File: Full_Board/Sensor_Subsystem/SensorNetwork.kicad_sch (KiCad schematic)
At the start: 32 parts, among them IC5 CD74HC4051PWT, IC6 CD74HC4051PWT, J10 OQ0432500000G, J11 OQ0432500000G, J12 OQ0432500000G, J13 OQ0432500000G, J14 OQ0432500000G, J15 OQ0432500000G, J16 OQ0432500000G, J17 OQ0432500000G, U10 UCLAMP3301H.TCT, U11 UCLAMP3301H.TCT

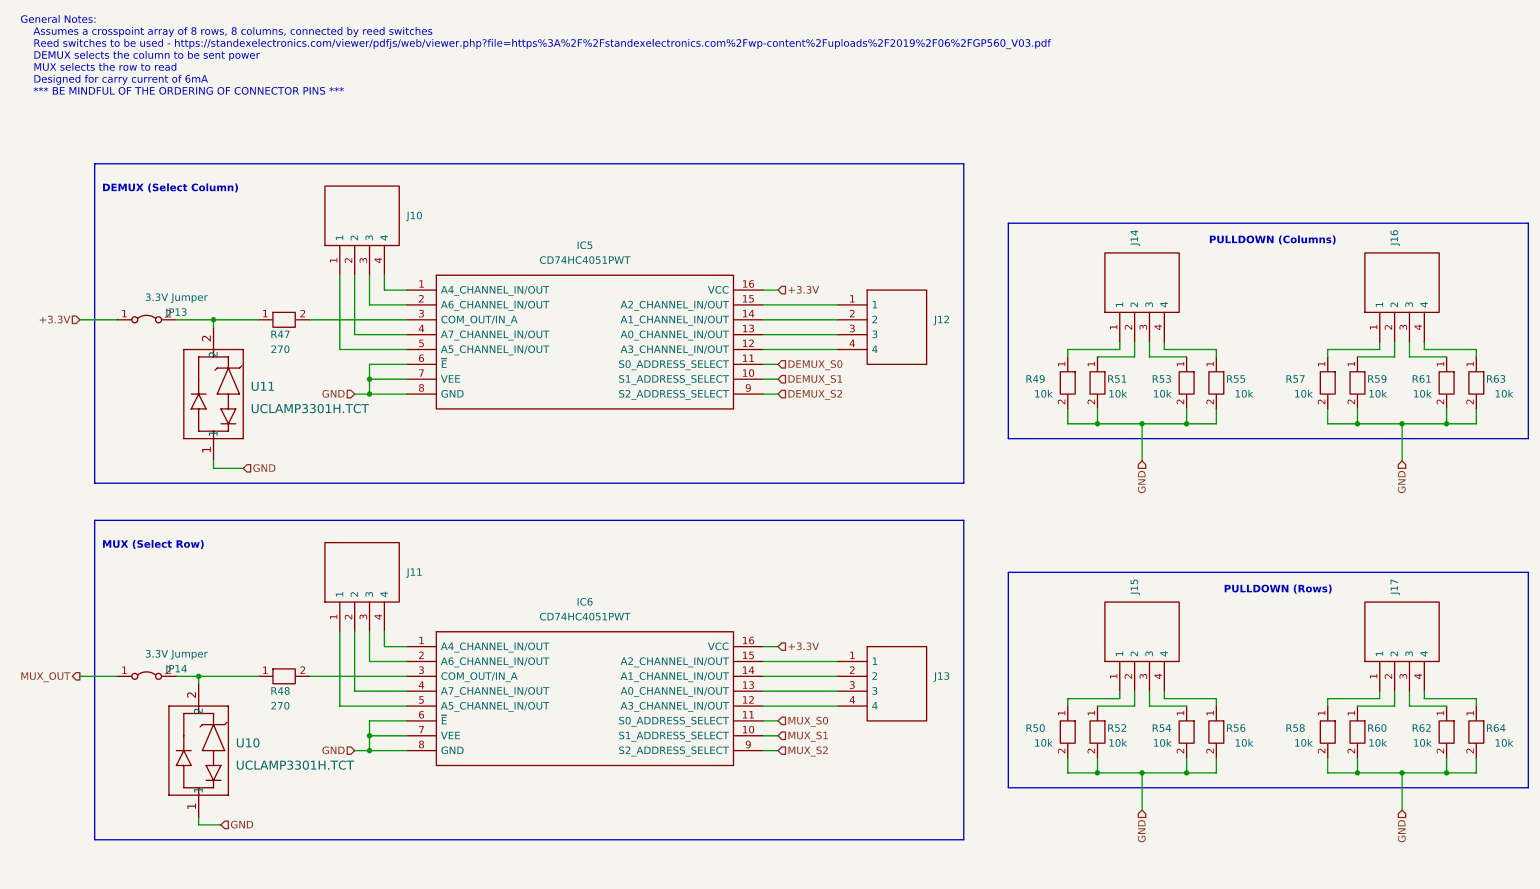
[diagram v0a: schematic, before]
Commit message: Redo pinout, finish pcb layout (no traces)
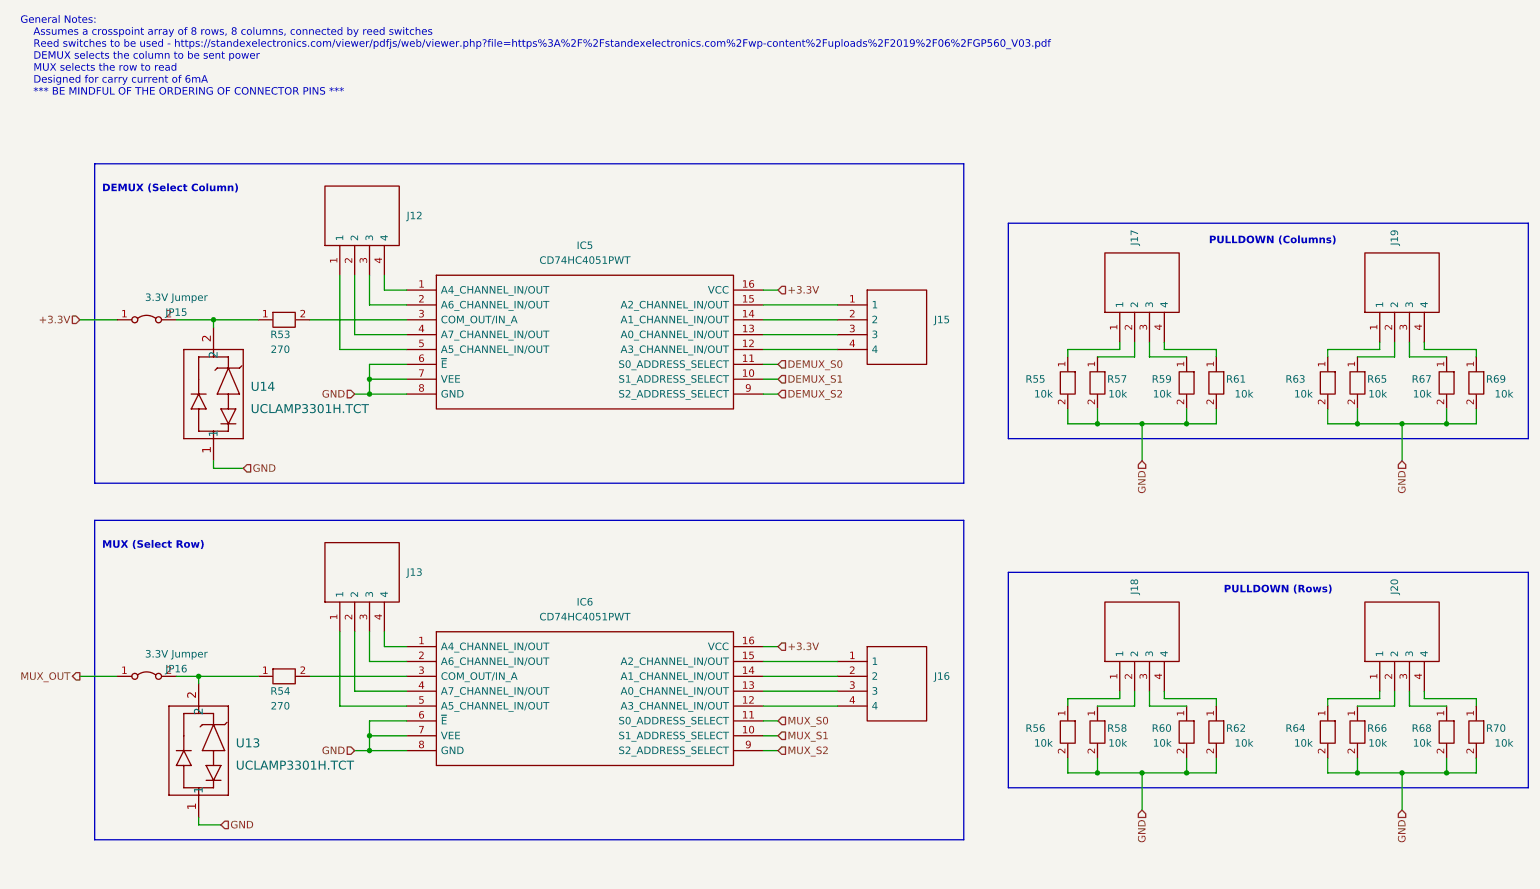
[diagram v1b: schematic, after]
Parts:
- renumbered J10 to J12, J11 to J13, J12 to J15, J13 to J16, J14 to J17, J15 to J18, J16 to J19, J17 to J20, JP13 to JP15, JP14 to JP16, R47 to R53, R48 to R54, R49 to R55, R50 to R56, R51 to R57, R52 to R58, R53 to R59, R54 to R60, R55 to R61, R56 to R62, R57 to R63, R58 to R64, R59 to R65, R60 to R66, R61 to R67, R62 to R68, R63 to R69, R64 to R70, U10 to U13, U11 to U14
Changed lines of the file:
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@@
   (symbol (lib_id "RMCF1206FT10K0:10k") (at 265.43 133.35 270) (unit 1)
     (in_bom yes) (on_board yes)
-    (property "Reference" "R64" (id 0) (at 270.51 137.16 90)
+    (property "Reference" "R70" (id 0) (at 270.51 137.16 90)
       (effects (font (size 1.27 1.27)) (justify right))
     )
@@
   (symbol (lib_id "RMCF1206FT10K0:10k") (at 260.35 133.35 270) (unit 1)
     (in_bom yes) (on_board yes)
-    (property "Reference" "R62" (id 0) (at 257.81 137.16 90)
+    (property "Reference" "R68" (id 0) (at 257.81 137.16 90)
       (effects (font (size 1.27 1.27)) (justify right))
     )
@@
   (symbol (lib_id "OQ04325500000G:OQ0432500000G") (at 156.21 125.73 0) (unit 1)
     (in_bom yes) (on_board yes) (fields_autoplaced)
-    (property "Reference" "J13" (id 0) (at 172.72 128.2699 0)
+    (property "Reference" "J16" (id 0) (at 172.72 128.2699 0)
       (effects (font (size 1.27 1.27)) (justify left))
     )
@@
   (symbol (lib_id "Jumper:Jumper_2_Bridged") (at 38.1 67.31 0) (unit 1)
     (in_bom yes) (on_board yes)
-    (property "Reference" "JP13" (id 0) (at 43.18 66.04 0))
+    (property "Reference" "JP15" (id 0) (at 43.18 66.04 0))
     (property "Value" "3.3V Jumper" (id 1) (at 43.18 63.5 0))
     (property "Footprint" "TestPoint:TestPoint_2Pads_Pitch2.54mm_Drill0.8mm" (id 2) (at 38.1 67.31 0)
@@
   (symbol (lib_id "RMCF1206FT10K0:10k") (at 260.35 73.66 270) (unit 1)
     (in_bom yes) (on_board yes)
-    (property "Reference" "R61" (id 0) (at 257.81 77.47 90)
+    (property "Reference" "R67" (id 0) (at 257.81 77.47 90)
       (effects (font (size 1.27 1.27)) (justify right))
     )
@@
   (symbol (lib_id "RMCF1206FT10K0:10k") (at 195.58 73.66 270) (unit 1)
     (in_bom yes) (on_board yes)
-    (property "Reference" "R49" (id 0) (at 191.77 77.47 90)
+    (property "Reference" "R55" (id 0) (at 191.77 77.47 90)
       (effects (font (size 1.27 1.27)) (justify right))
     )
@@
   (symbol (lib_id "Jumper:Jumper_2_Bridged") (at 38.1 128.27 0) (unit 1)
     (in_bom yes) (on_board yes)
-    (property "Reference" "JP14" (id 0) (at 43.18 127 0))
+    (property "Reference" "JP16" (id 0) (at 43.18 127 0))
     (property "Value" "3.3V Jumper" (id 1) (at 43.18 124.46 0))
     (property "Footprint" "TestPoint:TestPoint_2Pads_Pitch2.54mm_Drill0.8mm" (id 2) (at 38.1 128.27 0)
@@
   (symbol (lib_id "RMCF1206FT10K0:10k") (at 200.66 133.35 270) (unit 1)
     (in_bom yes) (on_board yes)
-    (property "Reference" "R52" (id 0) (at 205.74 137.16 90)
+    (property "Reference" "R58" (id 0) (at 205.74 137.16 90)
       (effects (font (size 1.27 1.27)) (justify right))
     )
@@
   (symbol (lib_id "OQ04325500000G:OQ0432500000G") (at 156.21 64.77 0) (unit 1)
     (in_bom yes) (on_board yes) (fields_autoplaced)
-    (property "Reference" "J12" (id 0) (at 172.72 67.3099 0)
+    (property "Reference" "J15" (id 0) (at 172.72 67.3099 0)
       (effects (font (size 1.27 1.27)) (justify left))
     )
@@
   (symbol (lib_id "SDR10EZPJ271:SDR10EZPJ271") (at 57.15 67.31 0) (unit 1)
     (in_bom yes) (on_board yes)
-    (property "Reference" "R47" (id 0) (at 60.96 69.85 0))
+    (property "Reference" "R53" (id 0) (at 60.96 69.85 0))
     (property "Value" "270" (id 1) (at 60.96 72.39 0))
     (property "Footprint" "SDR10EZPJ271:RESC2012X65N" (id 2) (at 71.12 66.04 0)
@@
   (symbol (lib_id "RMCF1206FT10K0:10k") (at 215.9 73.66 270) (unit 1)
     (in_bom yes) (on_board yes)
-    (property "Reference" "R53" (id 0) (at 213.36 77.47 90)
+    (property "Reference" "R59" (id 0) (at 213.36 77.47 90)
       (effects (font (size 1.27 1.27)) (justify right))
     )
@@
   (symbol (lib_id "RMCF1206FT10K0:10k") (at 265.43 73.66 270) (unit 1)
     (in_bom yes) (on_board yes)
-    (property "Reference" "R63" (id 0) (at 270.51 77.47 90)
+    (property "Reference" "R69" (id 0) (at 270.51 77.47 90)
       (effects (font (size 1.27 1.27)) (justify right))
     )
@@
   (symbol (lib_id "RMCF1206FT10K0:10k") (at 220.98 73.66 270) (unit 1)
     (in_bom yes) (on_board yes)
-    (property "Reference" "R55" (id 0) (at 226.06 77.47 90)
+    (property "Reference" "R61" (id 0) (at 226.06 77.47 90)
       (effects (font (size 1.27 1.27)) (justify right))
     )
@@
   (symbol (lib_id "UCLAMP3301H-TCT:UCLAMP3301H.TCT") (at 49.53 100.33 90) (unit 1)
     (in_bom yes) (on_board yes) (fields_autoplaced)
-    (property "Reference" "U11" (id 0) (at 55.88 78.74 90)
+    (property "Reference" "U14" (id 0) (at 55.88 78.74 90)
       (effects (font (size 1.524 1.524)) (justify right))
     )
@@
   (symbol (lib_id "RMCF1206FT10K0:10k") (at 245.11 73.66 270) (unit 1)
     (in_bom yes) (on_board yes)
-    (property "Reference" "R59" (id 0) (at 250.19 77.47 90)
+    (property "Reference" "R65" (id 0) (at 250.19 77.47 90)
       (effects (font (size 1.27 1.27)) (justify right))
     )
@@
   (symbol (lib_id "RMCF1206FT10K0:10k") (at 215.9 133.35 270) (unit 1)
     (in_bom yes) (on_board yes)
-    (property "Reference" "R54" (id 0) (at 213.36 137.16 90)
+    (property "Reference" "R60" (id 0) (at 213.36 137.16 90)
       (effects (font (size 1.27 1.27)) (justify right))
     )
@@
     (pin "2")
   )
-  (symbol (lib_name "UCLAMP3301H.TCT_1") (lib_id "UCLAMP3301H-TCT:UCLAMP3301H.TCT") (at 46.99 161.29 90) (unit 1)
+  (symbol (lib_id "UCLAMP3301H-TCT:UCLAMP3301H.TCT") (at 46.99 161.29 90) (unit 1)
     (in_bom yes) (on_board yes) (fields_autoplaced)
-    (property "Reference" "U10" (id 0) (at 53.34 139.7 90)
+    (property "Reference" "U13" (id 0) (at 53.34 139.7 90)
       (effects (font (size 1.524 1.524)) (justify right))
     )
@@
   (symbol (lib_id "OQ04325500000G:OQ0432500000G") (at 248.92 130.81 90) (unit 1)
     (in_bom yes) (on_board yes) (fields_autoplaced)
-    (property "Reference" "J17" (id 0) (at 251.4599 114.3 0)
+    (property "Reference" "J20" (id 0) (at 251.4599 114.3 0)
       (effects (font (size 1.27 1.27)) (justify left))
     )
@@
   (symbol (lib_id "RMCF1206FT10K0:10k") (at 200.66 73.66 270) (unit 1)
     (in_bom yes) (on_board yes)
-    (property "Reference" "R51" (id 0) (at 205.74 77.47 90)
+    (property "Reference" "R57" (id 0) (at 205.74 77.47 90)
       (effects (font (size 1.27 1.27)) (justify right))
     )
@@
   (symbol (lib_id "OQ04325500000G:OQ0432500000G") (at 204.47 130.81 90) (unit 1)
     (in_bom yes) (on_board yes) (fields_autoplaced)
-    (property "Reference" "J15" (id 0) (at 207.0099 114.3 0)
+    (property "Reference" "J18" (id 0) (at 207.0099 114.3 0)
       (effects (font (size 1.27 1.27)) (justify left))
     )
@@
   (symbol (lib_id "OQ04325500000G:OQ0432500000G") (at 248.92 71.12 90) (unit 1)
     (in_bom yes) (on_board yes) (fields_autoplaced)
-    (property "Reference" "J16" (id 0) (at 251.4599 54.61 0)
+    (property "Reference" "J19" (id 0) (at 251.4599 54.61 0)
       (effects (font (size 1.27 1.27)) (justify left))
     )
@@
   (symbol (lib_id "OQ04325500000G:OQ0432500000G") (at 71.12 120.65 90) (unit 1)
     (in_bom yes) (on_board yes) (fields_autoplaced)
-    (property "Reference" "J11" (id 0) (at 82.55 110.4899 90)
+    (property "Reference" "J13" (id 0) (at 82.55 110.4899 90)
       (effects (font (size 1.27 1.27)) (justify right))
     )
@@
   (symbol (lib_id "RMCF1206FT10K0:10k") (at 240.03 73.66 270) (unit 1)
     (in_bom yes) (on_board yes)
-    (property "Reference" "R57" (id 0) (at 236.22 77.47 90)
+    (property "Reference" "R63" (id 0) (at 236.22 77.47 90)
       (effects (font (size 1.27 1.27)) (justify right))
     )
@@
   (symbol (lib_id "RMCF1206FT10K0:10k") (at 245.11 133.35 270) (unit 1)
     (in_bom yes) (on_board yes)
-    (property "Reference" "R60" (id 0) (at 250.19 137.16 90)
+    (property "Reference" "R66" (id 0) (at 250.19 137.16 90)
       (effects (font (size 1.27 1.27)) (justify right))
     )
@@
   (symbol (lib_id "RMCF1206FT10K0:10k") (at 220.98 133.35 270) (unit 1)
     (in_bom yes) (on_board yes)
-    (property "Reference" "R56" (id 0) (at 226.06 137.16 90)
+    (property "Reference" "R62" (id 0) (at 226.06 137.16 90)
       (effects (font (size 1.27 1.27)) (justify right))
     )
@@
   (symbol (lib_id "SDR10EZPJ271:SDR10EZPJ271") (at 57.15 128.27 0) (unit 1)
     (in_bom yes) (on_board yes)
-    (property "Reference" "R48" (id 0) (at 60.96 130.81 0))
+    (property "Reference" "R54" (id 0) (at 60.96 130.81 0))
     (property "Value" "270" (id 1) (at 60.96 133.35 0))
     (property "Footprint" "SDR10EZPJ271:RESC2012X65N" (id 2) (at 71.12 127 0)
@@
   (symbol (lib_id "RMCF1206FT10K0:10k") (at 240.03 133.35 270) (unit 1)
     (in_bom yes) (on_board yes)
-    (property "Reference" "R58" (id 0) (at 236.22 137.16 90)
+    (property "Reference" "R64" (id 0) (at 236.22 137.16 90)
       (effects (font (size 1.27 1.27)) (justify right))
     )
@@
   (symbol (lib_id "OQ04325500000G:OQ0432500000G") (at 71.12 59.69 90) (unit 1)
     (in_bom yes) (on_board yes) (fields_autoplaced)
-    (property "Reference" "J10" (id 0) (at 82.55 49.5299 90)
+    (property "Reference" "J12" (id 0) (at 82.55 49.5299 90)
       (effects (font (size 1.27 1.27)) (justify right))
     )
@@
   (symbol (lib_id "RMCF1206FT10K0:10k") (at 195.58 133.35 270) (unit 1)
     (in_bom yes) (on_board yes)
-    (property "Reference" "R50" (id 0) (at 191.77 137.16 90)
+    (property "Reference" "R56" (id 0) (at 191.77 137.16 90)
       (effects (font (size 1.27 1.27)) (justify right))
     )
@@
   (symbol (lib_id "OQ04325500000G:OQ0432500000G") (at 204.47 71.12 90) (unit 1)
     (in_bom yes) (on_board yes) (fields_autoplaced)
-    (property "Reference" "J14" (id 0) (at 207.0099 54.61 0)
+    (property "Reference" "J17" (id 0) (at 207.0099 54.61 0)
       (effects (font (size 1.27 1.27)) (justify left))
     )

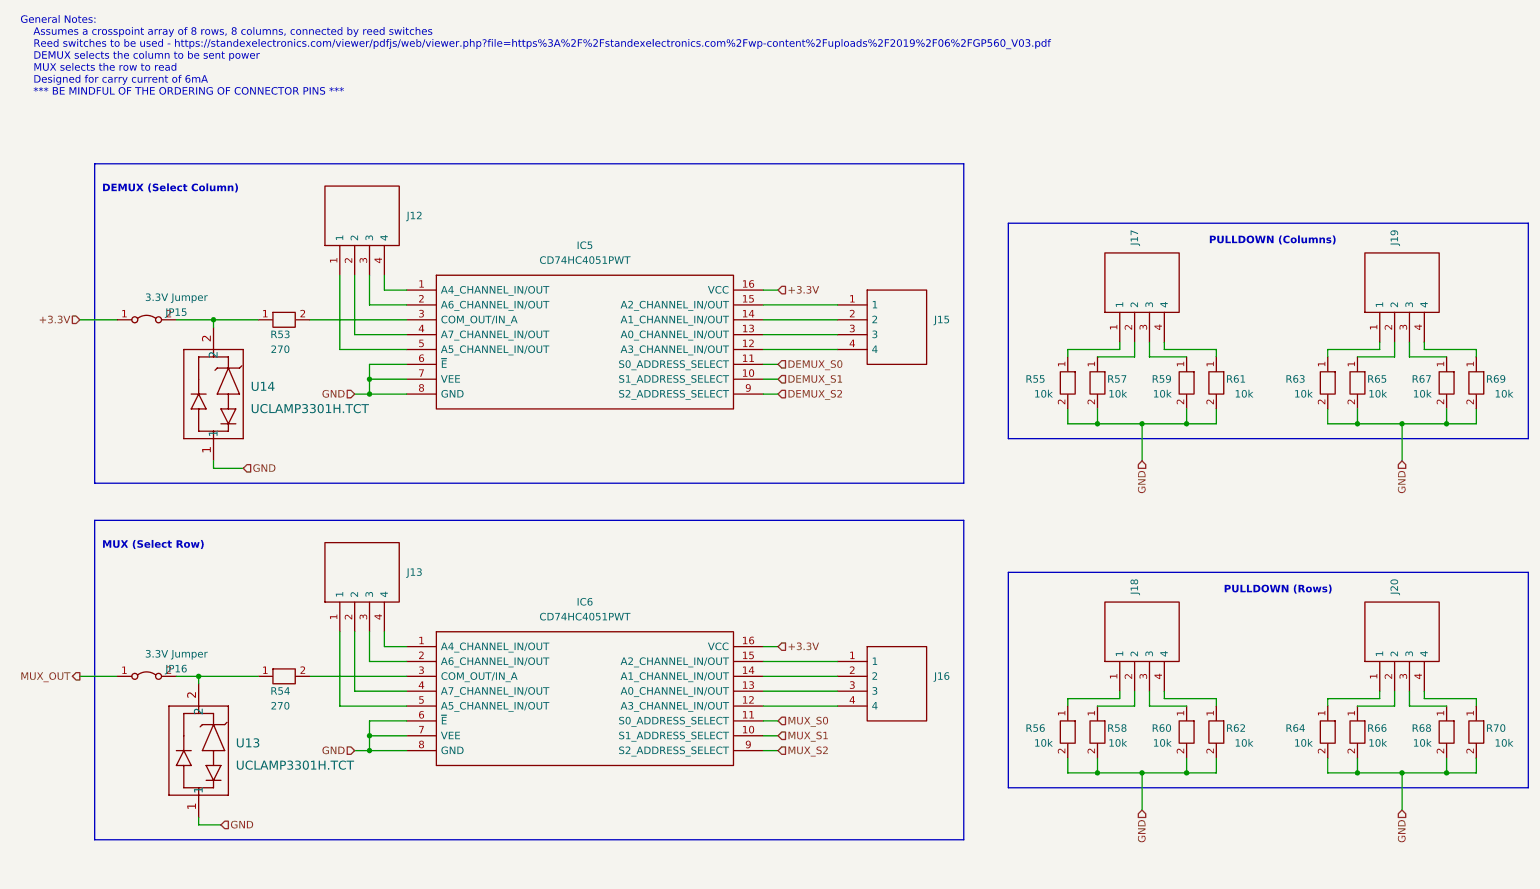
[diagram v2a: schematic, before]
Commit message: Fix vias for Analog Digital's requirements
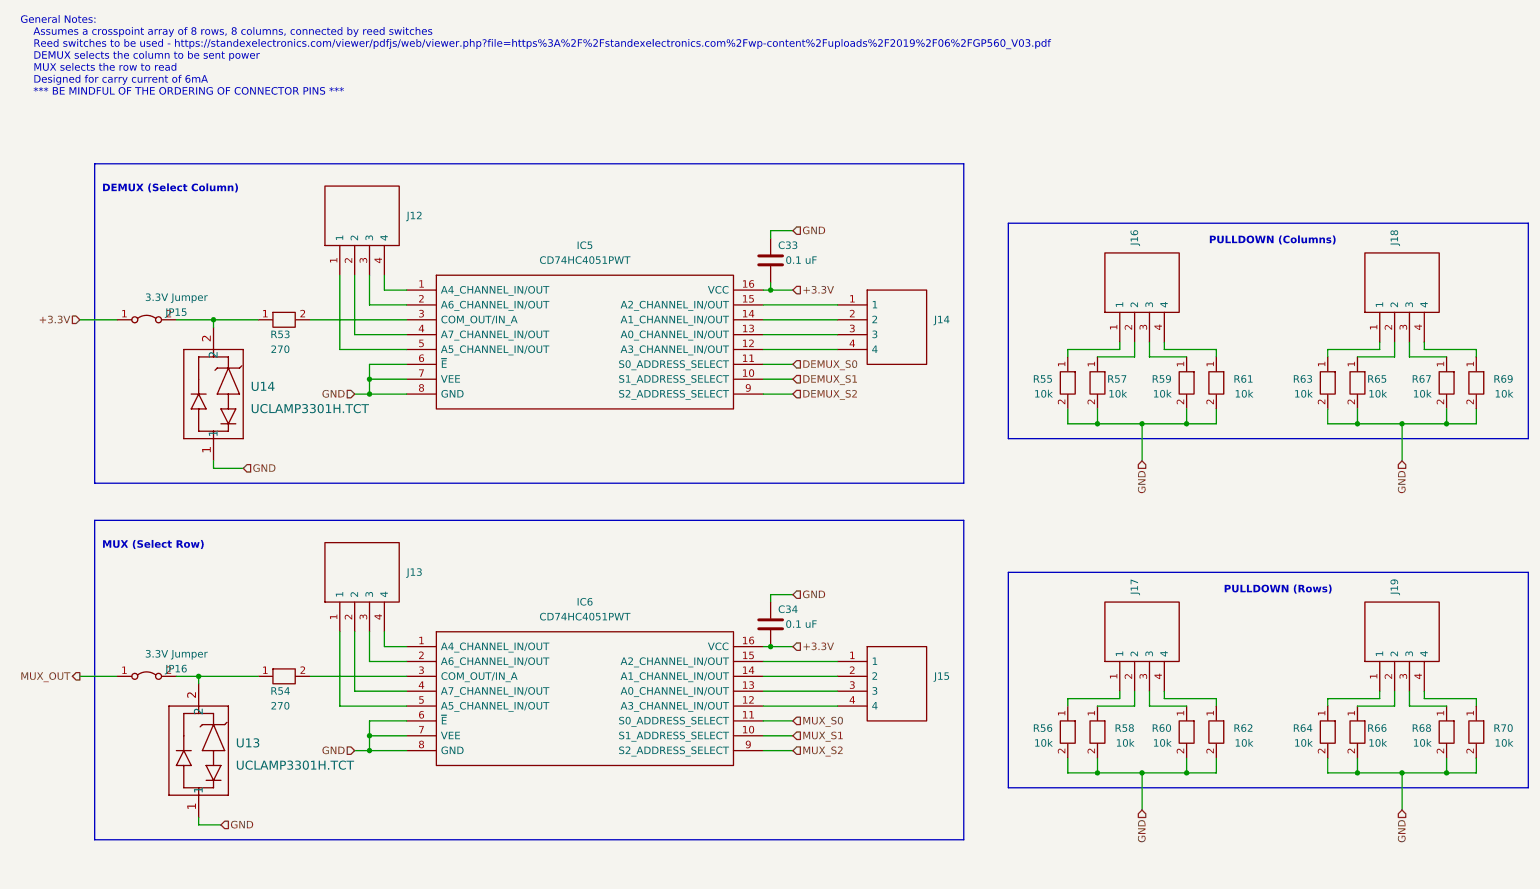
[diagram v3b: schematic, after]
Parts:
- added C33, C34: 0.1 uF, CL10B104KB8NNNC:CL10B104KB8NNNC, symbol Device:C
- renumbered J15 to J14, J16 to J15, J17 to J16, J18 to J17, J19 to J18, J20 to J19
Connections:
- net +3.3V: now also C33.2, C34.2
- net GND: now also C33.1, C34.1
